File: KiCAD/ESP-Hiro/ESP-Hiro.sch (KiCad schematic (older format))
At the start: 56 parts, among them J1 Conn_Q1, J2 Conn_Q2, J3 Conn_Q3, J4 Conn_Q4, J5 Conn_Q5, J6 Conn_ADC, Q1 AO3400A, Q2 AO3400A, Q3 AO3400A, Q4 AO3400A, Q5 AO3400A, U1 DHT22/DS18B20 header, U2 ESP-12E, U3 TPS54331D, U4 TLV75533PDBVR

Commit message: Fix schematic libraries
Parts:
- C1, C2, C3: symbol Smart-Home-Erweiterung-rescue:C_Small-device-Smart-Home-Erweiterung-rescue -> Device:C
- R1, R10, R19, R2, R20, R21, R22, R23, R3, R4, R5, R6, R7, R9: symbol Smart-Home-Erweiterung-rescue:R-device-Smart-Home-Erweiterung-rescue -> Device:R
- U1: symbol Smart-Home-Erweiterung-rescue:DHT11-Smart-Home-Erweiterung-rescue -> Sensor:DHT11
- U2: symbol Smart-Home-Erweiterung-rescue:ESP-12E-Smart-Home-Erweiterung-rescue -> ESP8266:ESP-12E
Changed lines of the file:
@@
 	1550 1800 1550 1950
 Wire Wire Line
-	1550 2250 1550 2350
+	1550 2300 1550 2350
 Wire Wire Line
 	2100 1950 1550 1950
 Connection ~ 1550 1950
 Wire Wire Line
-	1550 1950 1550 2050
+	1550 1950 1550 2000
 Text GLabel 3300 6050 0    47   Input ~ 0
 GPIO16
@@
 $EndComp
 $Comp
-L Smart-Home-Erweiterung-rescue:C_Small-device-Smart-Home-Erweiterung-rescue C?
+L Device:C C?
 U 1 1 6027D4E0
 P 1550 2150
@@
 $EndComp
 $Comp
-L Smart-Home-Erweiterung-rescue:C_Small-device-Smart-Home-Erweiterung-rescue C?
+L Device:C C?
 U 1 1 60280798
 P 1250 2150
@@
 	1150 1250 1250 1250
 Wire Wire Line
-	1250 2050 1250 1250
+	1250 2000 1250 1250
 Connection ~ 1250 1250
 Wire Wire Line
 	1250 1250 2100 1250
 Wire Wire Line
-	1250 2250 1250 2350
+	1250 2300 1250 2350
 Wire Wire Line
 	1250 2350 1400 2350
@@
 $EndComp
 $Comp
-L Smart-Home-Erweiterung-rescue:R-device-Smart-Home-Erweiterung-rescue R?
+L Device:R R?
 U 1 1 6025BA62
 P 4950 3750
@@
 $EndComp
 $Comp
-L Smart-Home-Erweiterung-rescue:R-device-Smart-Home-Erweiterung-rescue R?
+L Device:R R?
 U 1 1 601F651F
 P 4950 4250
@@
 $EndComp
 Wire Wire Line
-	2150 6900 2150 6800
-Wire Wire Line
-	2150 7600 2150 7500
-$Comp
-L power:+3.3V #PWR?
-U 1 1 602A00DE
-P 2150 6800
-AR Path="/601D55C5/602A00DE" Ref="#PWR?"  Part="1"
-AR Path="/602A00DE" Ref="#PWR05"  Part="1"
-F 0 "#PWR05" H 2150 6650 50  0001 C CNN
-F 1 "+3.3V" H 2150 6950 50  0000 C CNN
-F 2 "" H 2150 6800 50  0001 C CNN
-F 3 "" H 2150 6800 50  0001 C CNN
-	1    2150 6800
-	1    0    0    -1
-$EndComp
+	2050 7600 2050 7500
 Wire Wire Line
 	1650 7200 1750 7200
@@
 L power:GND #PWR?
 U 1 1 6029C38F
-P 2150 7600
+P 2050 7600
 AR Path="/601D55C5/6029C38F" Ref="#PWR?"  Part="1"
 AR Path="/6029C38F" Ref="#PWR06"  Part="1"
-F 0 "#PWR06" H 2150 7350 50  0001 C CNN
-F 1 "GND" H 2150 7450 50  0000 C CNN
-F 2 "" H 2150 7600 50  0001 C CNN
-F 3 "" H 2150 7600 50  0001 C CNN
-	1    2150 7600
+F 0 "#PWR06" H 2050 7350 50  0001 C CNN
+F 1 "GND" H 2050 7450 50  0000 C CNN
+F 2 "" H 2050 7600 50  0001 C CNN
+F 3 "" H 2050 7600 50  0001 C CNN
+	1    2050 7600
 	1    0    0    -1
 $EndComp
 Text GLabel 1650 7200 0    60   Input ~ 0
 GPIO2
-$Comp
-L Smart-Home-Erweiterung-rescue:DHT11-Smart-Home-Erweiterung-rescue U?
-U 1 1 6029C388
-P 2050 7200
-AR Path="/601D55C5/6029C388" Ref="U?"  Part="1"
-AR Path="/6029C388" Ref="U1"  Part="1"
-F 0 "U1" H 2200 7450 50  0000 C CNN
-F 1 "DHT22/DS18B20 header" H 2450 7550 50  0000 C CNN
-F 2 "Sensors:DHT22_Temperature_Humidity" H 2200 7450 50  0001 C CNN
-F 3 "" H 2200 7450 50  0001 C CNN
-	1    2050 7200
-	-1   0    0    -1
-$EndComp
 Wire Wire Line
 	2000 3850 1800 3850
@@
 SCL
 $Comp
-L Smart-Home-Erweiterung-rescue:R-device-Smart-Home-Erweiterung-rescue R?
+L Device:R R?
 U 1 1 602700E8
 P 1650 3850
@@
 $EndComp
 $Comp
-L Smart-Home-Erweiterung-rescue:R-device-Smart-Home-Erweiterung-rescue R?
+L Device:R R?
 U 1 1 6026FF3D
 P 1650 4000
@@
 $EndComp
 $Comp
-L Smart-Home-Erweiterung-rescue:R-device-Smart-Home-Erweiterung-rescue R?
+L Device:R R?
 U 1 1 6025CD2E
 P 1650 5100
@@
 $EndComp
 $Comp
-L Smart-Home-Erweiterung-rescue:R-device-Smart-Home-Erweiterung-rescue R?
+L Device:R R?
 U 1 1 6025CB7B
 P 1650 4600
@@
 $EndComp
 $Comp
-L Smart-Home-Erweiterung-rescue:R-device-Smart-Home-Erweiterung-rescue R?
+L Device:R R?
 U 1 1 6025C99C
 P 1650 4450
@@
 $EndComp
 $Comp
-L Smart-Home-Erweiterung-rescue:R-device-Smart-Home-Erweiterung-rescue R?
+L Device:R R?
 U 1 1 6025C725
 P 1650 4300
@@
 $EndComp
 $Comp
-L Smart-Home-Erweiterung-rescue:R-device-Smart-Home-Erweiterung-rescue R?
+L Device:R R?
 U 1 1 6025C0CA
 P 1650 4150
@@
 	1300 4150 1300 4300
 Wire Wire Line
-	1550 4850 1300 4850
-Wire Wire Line
-	1900 4850 1750 4850
+	1500 4850 1300 4850
+Wire Wire Line
+	1900 4850 1800 4850
 Wire Wire Line
 	1900 4600 1900 4850
@@
 Pullup/-down
 $Comp
-L Smart-Home-Erweiterung-rescue:C_Small-device-Smart-Home-Erweiterung-rescue C?
+L Device:C C?
 U 1 1 601FDA62
 P 1650 4850
 AR Path="/601D55C5/601FDA62" Ref="C?"  Part="1"
 AR Path="/601FDA62" Ref="C3"  Part="1"
-F 0 "C3" V 1550 4800 50  0000 L CNN
-F 1 "100nF" V 1750 4750 50  0000 L CNN
+F 0 "C3" V 1600 4900 50  0000 L CNN
+F 1 "100nF" V 1700 4900 50  0000 L CNN
 F 2 "Capacitor_SMD:C_0603_1608Metric" H 1650 4850 50  0001 C CNN
 F 3 "" H 1650 4850 50  0001 C CNN
@@
 $EndComp
 $Comp
-L Smart-Home-Erweiterung-rescue:R-device-Smart-Home-Erweiterung-rescue R?
+L Device:R R?
 U 1 1 6030A7D3
 P 13950 3650
@@
 $EndComp
 $Comp
-L Smart-Home-Erweiterung-rescue:R-device-Smart-Home-Erweiterung-rescue R?
+L Device:R R?
 U 1 1 6033B84E
 P 13950 2100
@@
 $EndComp
 $Comp
-L Smart-Home-Erweiterung-rescue:R-device-Smart-Home-Erweiterung-rescue R?
+L Device:R R?
 U 1 1 6034834A
 P 13950 5200
@@
 $EndComp
 $Comp
-L Smart-Home-Erweiterung-rescue:R-device-Smart-Home-Erweiterung-rescue R?
+L Device:R R?
 U 1 1 60353029
 P 13950 6750
@@
 $EndComp
 $Comp
-L Smart-Home-Erweiterung-rescue:R-device-Smart-Home-Erweiterung-rescue R?
+L Device:R R?
 U 1 1 6035EA25
 P 13950 8300
@@
 	3900 1250 4000 1250
 $Comp
-L Smart-Home-Erweiterung-rescue:ESP-12E-Smart-Home-Erweiterung-rescue U?
+L ESP8266:ESP-12E U?
 U 1 1 60207857
 P 3000 1550
@@
 Text Notes 4700 3350 0    47   ~ 0
 ADC
+$Comp
+L power:+3.3V #PWR?
+U 1 1 602A00DE
+P 2050 6800
+AR Path="/601D55C5/602A00DE" Ref="#PWR?"  Part="1"
+AR Path="/602A00DE" Ref="#PWR05"  Part="1"
+F 0 "#PWR05" H 2050 6650 50  0001 C CNN
+F 1 "+3.3V" H 2050 6950 50  0000 C CNN
+F 2 "" H 2050 6800 50  0001 C CNN
+F 3 "" H 2050 6800 50  0001 C CNN
+	1    2050 6800
+	1    0    0    -1
+$EndComp
+Wire Wire Line
+	2050 6900 2050 6800
+$Comp
+L Sensor:DHT11 U?
+U 1 1 6029C388
+P 2050 7200
+AR Path="/601D55C5/6029C388" Ref="U?"  Part="1"
+AR Path="/6029C388" Ref="U1"  Part="1"
+F 0 "U1" H 2200 7450 50  0000 C CNN
+F 1 "DHT22/DS18B20 header" H 2550 7550 50  0000 C CNN
+F 2 "Sensors:DHT22_Temperature_Humidity" H 2200 7450 50  0001 C CNN
+F 3 "" H 2200 7450 50  0001 C CNN
+	1    2050 7200
+	-1   0    0    -1
+$EndComp
 $EndSCHEMATC

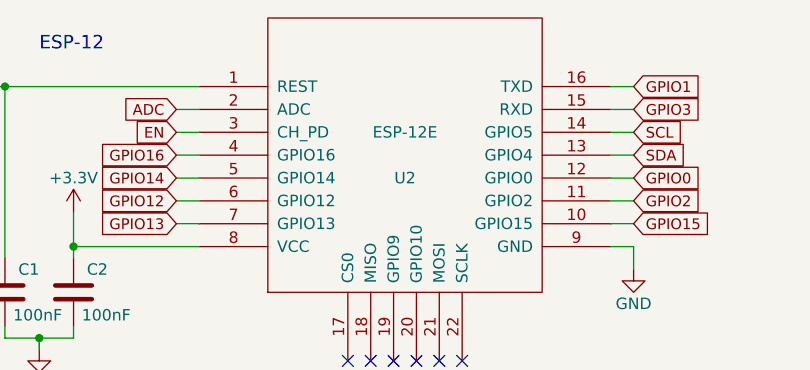
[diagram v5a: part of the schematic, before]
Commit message: Remove rescue lib references
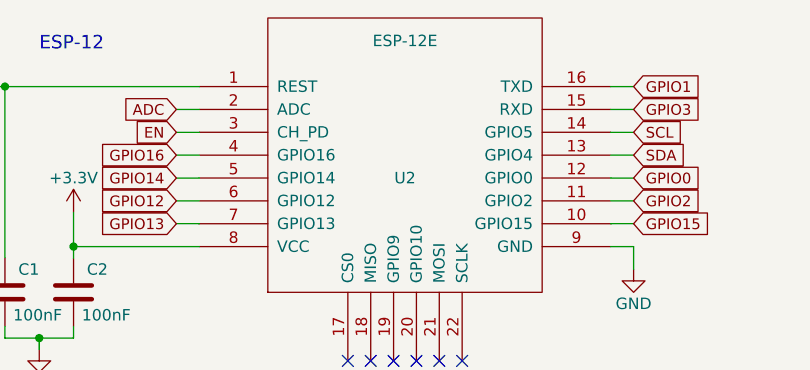
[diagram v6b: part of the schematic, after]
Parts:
- J6: LCSC (none) -> C577535
- U2: LCSC (none) -> C82891
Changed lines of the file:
@@
 AR Path="/60207857" Ref="U2"  Part="1"
 F 0 "U2" H 3000 1450 50  0000 C CNN
-F 1 "ESP-12E" H 3000 1650 50  0000 C CNN
+F 1 "ESP-12E" H 3000 2050 50  0000 C CNN
 F 2 "ESP8266:ESP-12E_SMD" H 3000 1550 50  0001 C CNN
 F 3 "" H 3000 1550 50  0001 C CNN
+F 4 "C82891" H 3000 1550 50  0001 C CNN "LCSC"
 	1    3000 1550
 	1    0    0    -1
@@
 F 2 "" H 4450 4050 50  0001 C CNN
 F 3 "~" H 4450 4050 50  0001 C CNN
+F 4 "C577535" H 4450 4050 50  0001 C CNN "LCSC"
 	1    4450 4050
 	-1   0    0    1

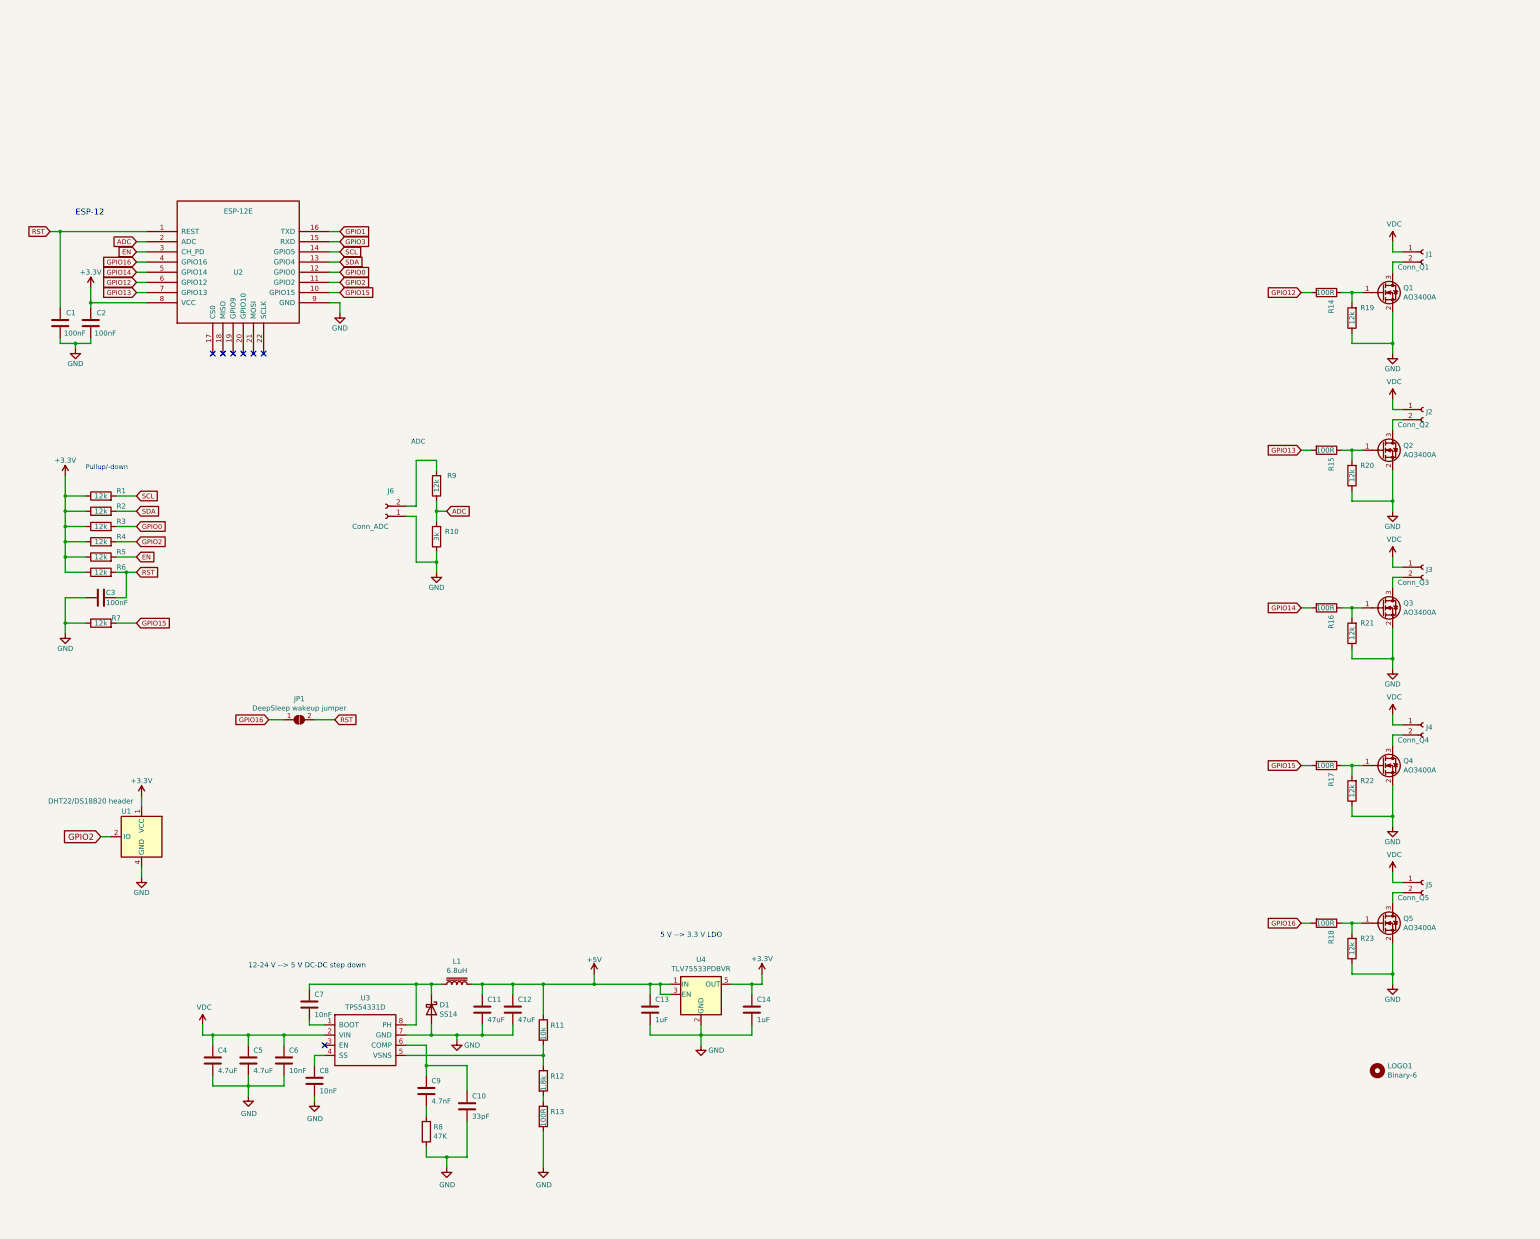
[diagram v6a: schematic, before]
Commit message: Add USB interface to schematic
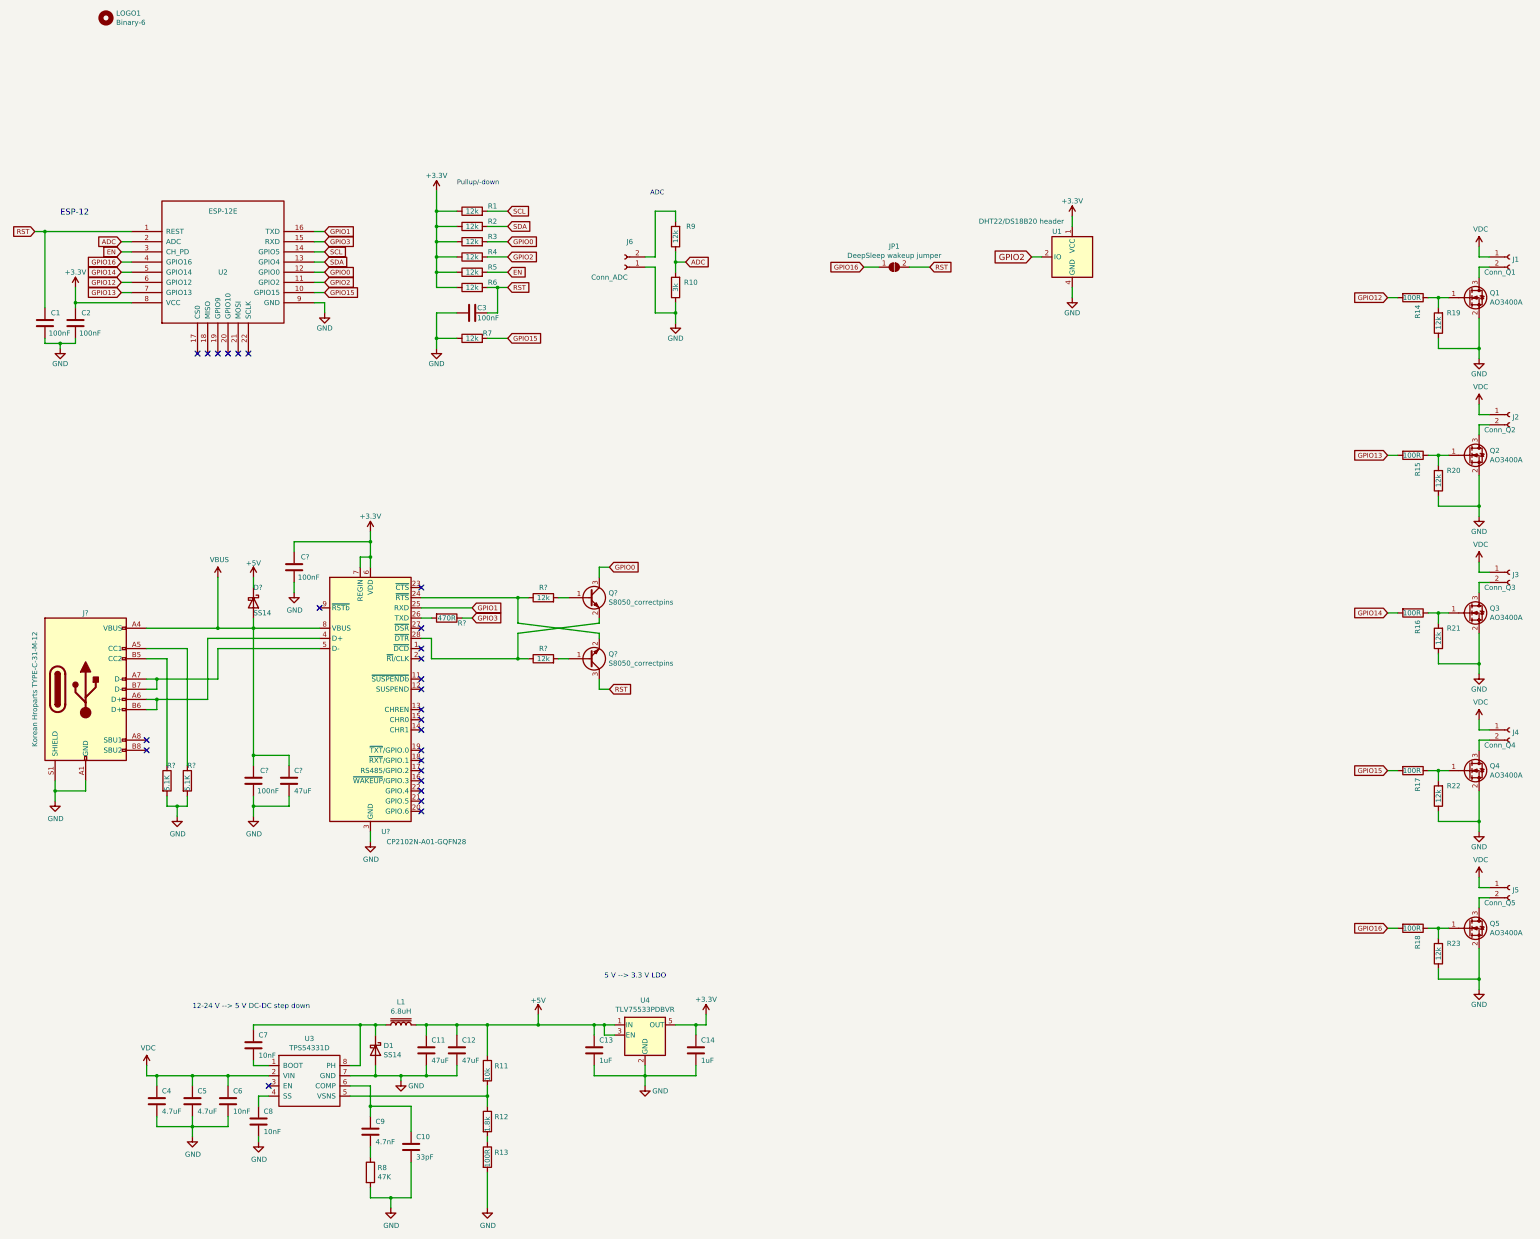
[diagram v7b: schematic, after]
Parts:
- added C? (x2): 100nF, Capacitor_SMD:C_0603_1608Metric, symbol Device:C
- added C?: 47uF, Capacitor_SMD:C_1206_3216Metric, symbol Device:C
- added D?: SS14, Diode_SMD:D_SMA, symbol MeineBibli:SS14
- added J?: Korean Hroparts TYPE-C-31-M-12, Connector_USB:USB_C_Receptacle_HRO_TYPE-C-31-M-12, symbol Connector:USB_C_Receptacle_USB2.0
- added Q? (x2): S8050_correctpins, Package_TO_SOT_SMD:SOT-23, symbol MeineBibli:S8050_correctpins
- added R?: 470R, Resistor_SMD:R_0603_1608Metric, symbol Device:R
- added R? (x2): 12k, Resistor_SMD:R_0603_1608Metric, symbol Device:R
- added R? (x2): 5.1K, Resistor_SMD:R_0603_1608Metric, symbol Device:R
- added U?: CP2102N-A01-GQFN28, Package_DFN_QFN:QFN-28-1EP_5x5mm_P0.5mm_EP3.35x3.35mm, symbol Interface_USB:CP2102N-A01-GQFN28
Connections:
- net +3V3: now also C?.2, U?.6 (VDD), U?.7 (REGIN)
- net +5V: now also D?.1 (K)
- net GND: now also C?.1, C?.1, C?.2, J?.A1 (GND), J?.A12 (GND), J?.B1 (GND), J?.B12 (GND), J?.S1 (SHIELD), R?.2, R?.2, U?.29 (GND), U?.3 (GND)
- net GPIO0: now also Q?.3 (C)
- net GPIO1: now also U?.25 (RXD)
- net GPIO3: now also R?.1
- net RST: now also Q?.3 (C)
- new net: J?.A5 (CC1), R?.1
- new net: J?.A6 (D+), J?.B6 (D+), U?.4 (D+)
- new net: J?.A7 (D-), J?.B7 (D-), U?.5 (D-)
- new net: J?.B5 (CC2), R?.1
- new net: Q?.2 (E), R?.1, U?.24 (~RTS)
- new net: R?.2, U?.26 (TXD)
- new net: Q?.2 (E), R?.1, U?.28 (~DTR)
- new net: Q?.1 (B), R?.2 (x2)
- new net VBUS: C?.1, C?.2, D?.2 (A), J?.A4 (VBUS), J?.A9 (VBUS), J?.B4 (VBUS), J?.B9 (VBUS), U?.8 (VBUS)
- no-connect marks 7 -> 26
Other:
- moved on the sheet: C1, C10, C11, C12, C13, C14, C2, C3, C4, C5, C6, C7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
